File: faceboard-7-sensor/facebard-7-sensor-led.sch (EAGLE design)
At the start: 31 parts, among them Q1 QRE1113, Q2 QRE1113, Q3 QRE1113, Q4 QRE1113, Q5 QRE1113, Q6 QRE1113, Q7 QRE1113, U1 CD4051BE

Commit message: add ffc boards
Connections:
- net N$10 renamed C4
- net N$12 renamed C5
- net N$14 renamed C6
- net N$2 renamed C0
- net N$4 renamed C1
- net N$6 renamed C2
- net N$8 renamed C3
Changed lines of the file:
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@@
 </segment>
 </net>
-<net name="N$2" class="0">
+<net name="C0" class="0">
 <segment>
 <wire x1="20.32" y1="86.36" x2="124.46" y2="86.36" width="0.1524" layer="91"/>
@@
 <wire x1="22.86" y1="157.48" x2="20.32" y2="157.48" width="0.1524" layer="91"/>
 <junction x="22.86" y="157.48"/>
+<label x="124.46" y="63.5" size="1.778" layer="95" xref="yes"/>
 </segment>
 </net>
@@
 </segment>
 </net>
-<net name="N$4" class="0">
+<net name="C1" class="0">
 <segment>
 <pinref part="Q2" gate="A" pin="3"/>
@@
 <wire x1="137.16" y1="93.98" x2="137.16" y2="66.04" width="0.1524" layer="91"/>
 <wire x1="137.16" y1="66.04" x2="109.22" y2="66.04" width="0.1524" layer="91"/>
+<label x="137.16" y="66.04" size="1.778" layer="95" xref="yes"/>
 </segment>
 </net>
@@
 </segment>
 </net>
-<net name="N$6" class="0">
+<net name="C2" class="0">
 <segment>
 <pinref part="Q3" gate="A" pin="3"/>
@@
 <pinref part="U1" gate="A" pin="CHANNELSIN/OUT2"/>
 <wire x1="162.56" y1="68.58" x2="109.22" y2="68.58" width="0.1524" layer="91"/>
+<label x="132.08" y="68.58" size="1.778" layer="95" rot="R90" xref="yes"/>
 </segment>
 </net>
@@
 </segment>
 </net>
-<net name="N$8" class="0">
+<net name="C3" class="0">
 <segment>
 <pinref part="Q4" gate="A" pin="3"/>
@@
 <wire x1="228.6" y1="60.96" x2="109.22" y2="60.96" width="0.1524" layer="91"/>
 <junction x="228.6" y="157.48"/>
+<label x="132.08" y="63.5" size="1.778" layer="95" rot="R270" xref="yes"/>
 </segment>
 </net>
@@
 </segment>
 </net>
-<net name="N$10" class="0">
+<net name="C4" class="0">
 <segment>
 <pinref part="Q5" gate="A" pin="3"/>
@@
 <pinref part="U1" gate="A" pin="CHANNELSIN/OUT4"/>
 <wire x1="2.54" y1="71.12" x2="7.62" y2="71.12" width="0.1524" layer="91"/>
+<label x="5.08" y="71.12" size="1.778" layer="95" rot="R90" xref="yes"/>
 </segment>
 </net>
@@
 </segment>
 </net>
-<net name="N$12" class="0">
+<net name="C5" class="0">
 <segment>
 <pinref part="Q6" gate="A" pin="3"/>
@@
 <wire x1="-5.08" y1="78.74" x2="-5.08" y2="60.96" width="0.1524" layer="91"/>
 <wire x1="-5.08" y1="60.96" x2="7.62" y2="60.96" width="0.1524" layer="91"/>
+<label x="0" y="60.96" size="1.778" layer="95" rot="R270" xref="yes"/>
 </segment>
 </net>
@@
 </segment>
 </net>
-<net name="N$14" class="0">
+<net name="C6" class="0">
 <segment>
 <pinref part="Q7" gate="A" pin="3"/>
@@
 <wire x1="424.18" y1="147.32" x2="426.72" y2="147.32" width="0.1524" layer="91"/>
 <wire x1="426.72" y1="147.32" x2="426.974" y2="80.518" width="0.1524" layer="91"/>
-<wire x1="426.974" y1="80.518" x2="0.254" y2="80.518" width="0.1524" layer="91"/>
-<wire x1="0.254" y1="80.518" x2="0" y2="68.58" width="0.1524" layer="91"/>
+<wire x1="426.974" y1="80.518" x2="0" y2="81.026" width="0.1524" layer="91"/>
+<wire x1="0" y1="81.026" x2="0" y2="68.58" width="0.1524" layer="91"/>
 <pinref part="U1" gate="A" pin="CHANNELSIN/OUT6"/>
 <wire x1="0" y1="68.58" x2="7.62" y2="68.58" width="0.1524" layer="91"/>
-</segment>
-</net>
+<label x="0" y="68.58" size="1.778" layer="95" rot="R180" xref="yes"/>
+</segment>
+</net>

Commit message: routing
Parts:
- SV2: SPICEPREFIX (none) -> X
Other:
- moved on the sheet: D1, D2, D3, D4, D5, D6, D7, U1

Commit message: re-draw schematics
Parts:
- R10: value 10k -> 100k
- SV2: value header -> Output
- SV3: value header -> Input
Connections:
- net LEDDIN renamed N$12
- new net N$14: D1.VSS, D2.VSS, D3.VSS
- new net N$15: D4.VSS
- new net VCC: R1.1, R10.2, R11.1, R12.2, R13.1, R14.2, R2.2, R3.1, R4.2, R5.1, R6.2, R7.1, R8.2, R9.1, SV2.2, SV3.2
- net 5V: no longer R1.1, R10.2, R11.1, R12.2, R13.1, R14.2, R2.2, R3.1, R4.2, R5.1, R6.2, R7.1, R8.2, R9.1, SV2.2, SV3.2
- net C0: now also U1.CH0; no longer U1.CHANNELSIN/OUT0
- net C1: now also U1.CH1; no longer U1.CHANNELSIN/OUT1
- net C2: now also U1.CH2; no longer U1.CHANNELSIN/OUT2
- net C3: now also U1.CH3; no longer U1.CHANNELSIN/OUT3
- net C4: now also U1.CH4; no longer U1.CHANNELSIN/OUT4
- net C5: now also U1.CH5; no longer U1.CHANNELSIN/OUT5
- net C6: now also U1.CH6; no longer U1.CHANNELSIN/OUT6
- net GND: now also U1.GND; no longer D1.VSS, D2.VSS, D3.VSS, D4.VSS, U1.VSS
- net SIG: now also U1.COM; no longer U1.COMOUT/IN
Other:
- moved on the sheet: D1, D2, D3, D4, D5, D6, D7, R1, R10, R11, R12, R13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

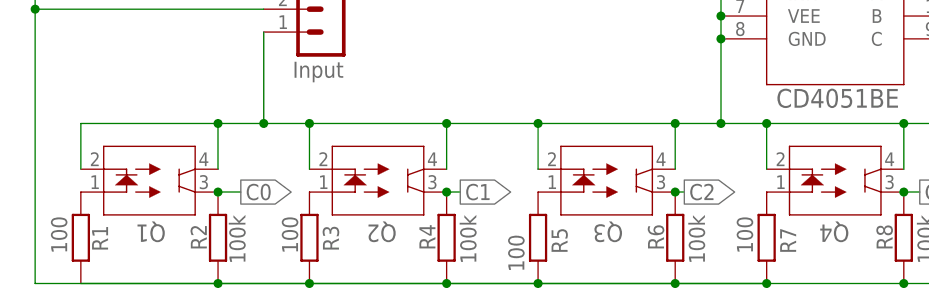
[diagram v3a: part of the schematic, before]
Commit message: fix vcc net
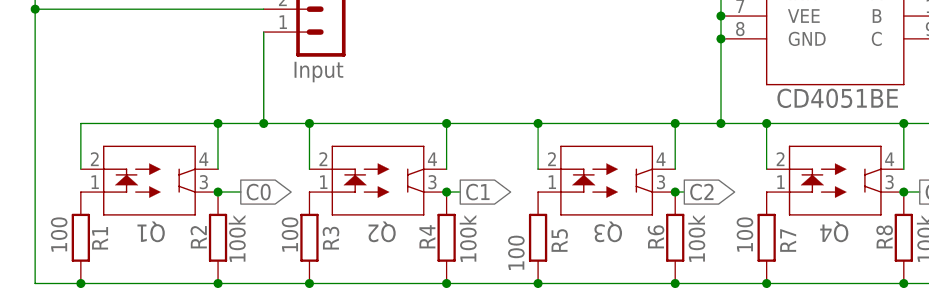
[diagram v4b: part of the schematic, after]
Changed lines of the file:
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@@
 <net name="VCC" class="0">
 <segment>
+<pinref part="SUPPLY2" gate="G$1" pin="VCC"/>
+<wire x1="-22.86" y1="91.44" x2="-22.86" y2="132.08" width="0.1524" layer="91"/>
+<pinref part="SV3" gate="1" pin="2"/>
+<wire x1="2.54" y1="91.44" x2="-22.86" y2="91.44" width="0.1524" layer="91"/>
+<junction x="-22.86" y="91.44"/>
+<wire x1="-22.86" y1="60.96" x2="-22.86" y2="91.44" width="0.1524" layer="91"/>
+<wire x1="162.56" y1="91.44" x2="162.56" y2="60.96" width="0.1524" layer="91"/>
+<pinref part="SV2" gate="1" pin="2"/>
+<wire x1="162.56" y1="91.44" x2="129.54" y2="91.44" width="0.1524" layer="91"/>
+<wire x1="162.56" y1="60.96" x2="149.86" y2="60.96" width="0.1524" layer="91"/>
 <pinref part="R1" gate="G$1" pin="1"/>
-<wire x1="-17.78" y1="60.96" x2="-2.54" y2="60.96" width="0.1524" layer="91"/>
-<pinref part="R2" gate="G$1" pin="2"/>
-<junction x="-2.54" y="60.96"/>
-<wire x1="-2.54" y1="60.96" x2="7.62" y2="60.96" width="0.1524" layer="91"/>
-<pinref part="R3" gate="G$1" pin="1"/>
-<junction x="7.62" y="60.96"/>
-<wire x1="7.62" y1="60.96" x2="22.86" y2="60.96" width="0.1524" layer="91"/>
-<pinref part="R4" gate="G$1" pin="2"/>
-<junction x="22.86" y="60.96"/>
-<wire x1="22.86" y1="60.96" x2="33.02" y2="60.96" width="0.1524" layer="91"/>
-<pinref part="R5" gate="G$1" pin="1"/>
-<junction x="33.02" y="60.96"/>
-<wire x1="33.02" y1="60.96" x2="48.26" y2="60.96" width="0.1524" layer="91"/>
-<pinref part="R6" gate="G$1" pin="2"/>
-<junction x="48.26" y="60.96"/>
-<wire x1="48.26" y1="60.96" x2="58.42" y2="60.96" width="0.1524" layer="91"/>
-<pinref part="R7" gate="G$1" pin="1"/>
-<junction x="58.42" y="60.96"/>
-<wire x1="58.42" y1="60.96" x2="-22.86" y2="60.96" width="0.1524" layer="91"/>
-<pinref part="R14" gate="G$1" pin="2"/>
 <wire x1="149.86" y1="60.96" x2="134.62" y2="60.96" width="0.1524" layer="91"/>
-<pinref part="R13" gate="G$1" pin="1"/>
 <wire x1="134.62" y1="60.96" x2="124.46" y2="60.96" width="0.1524" layer="91"/>
 <wire x1="124.46" y1="60.96" x2="109.22" y2="60.96" width="0.1524" layer="91"/>
@@
 <wire x1="83.82" y1="60.96" x2="73.66" y2="60.96" width="0.1524" layer="91"/>
 <wire x1="73.66" y1="60.96" x2="58.42" y2="60.96" width="0.1524" layer="91"/>
-<junction x="134.62" y="60.96"/>
+<wire x1="58.42" y1="60.96" x2="48.26" y2="60.96" width="0.1524" layer="91"/>
+<wire x1="48.26" y1="60.96" x2="33.02" y2="60.96" width="0.1524" layer="91"/>
+<wire x1="33.02" y1="60.96" x2="22.86" y2="60.96" width="0.1524" layer="91"/>
+<wire x1="22.86" y1="60.96" x2="7.62" y2="60.96" width="0.1524" layer="91"/>
+<wire x1="7.62" y1="60.96" x2="-2.54" y2="60.96" width="0.1524" layer="91"/>
+<wire x1="-2.54" y1="60.96" x2="-17.78" y2="60.96" width="0.1524" layer="91"/>
+<wire x1="-17.78" y1="60.96" x2="-22.86" y2="60.96" width="0.1524" layer="91"/>
+<junction x="-17.78" y="60.96"/>
+<pinref part="R2" gate="G$1" pin="2"/>
+<junction x="-2.54" y="60.96"/>
+<pinref part="R3" gate="G$1" pin="1"/>
+<junction x="7.62" y="60.96"/>
+<pinref part="R4" gate="G$1" pin="2"/>
+<junction x="22.86" y="60.96"/>
+<pinref part="R5" gate="G$1" pin="1"/>
+<junction x="33.02" y="60.96"/>
+<pinref part="R6" gate="G$1" pin="2"/>
+<junction x="48.26" y="60.96"/>
+<pinref part="R7" gate="G$1" pin="1"/>
+<junction x="58.42" y="60.96"/>
+<pinref part="R8" gate="G$1" pin="2"/>
+<junction x="73.66" y="60.96"/>
+<pinref part="R9" gate="G$1" pin="1"/>
+<junction x="83.82" y="60.96"/>
+<pinref part="R10" gate="G$1" pin="2"/>
+<junction x="99.06" y="60.96"/>
+<pinref part="R11" gate="G$1" pin="1"/>
+<junction x="109.22" y="60.96"/>
 <pinref part="R12" gate="G$1" pin="2"/>
 <junction x="124.46" y="60.96"/>
-<pinref part="R11" gate="G$1" pin="1"/>
-<junction x="109.22" y="60.96"/>
-<pinref part="R10" gate="G$1" pin="2"/>
-<junction x="99.06" y="60.96"/>
-<pinref part="R9" gate="G$1" pin="1"/>
-<junction x="83.82" y="60.96"/>
-<pinref part="R8" gate="G$1" pin="2"/>
-<junction x="73.66" y="60.96"/>
-<pinref part="SUPPLY2" gate="G$1" pin="VCC"/>
-<wire x1="-22.86" y1="60.96" x2="-22.86" y2="91.44" width="0.1524" layer="91"/>
-<pinref part="SV3" gate="1" pin="2"/>
-<wire x1="-22.86" y1="91.44" x2="-22.86" y2="132.08" width="0.1524" layer="91"/>
-<wire x1="2.54" y1="91.44" x2="-22.86" y2="91.44" width="0.1524" layer="91"/>
-<junction x="-22.86" y="91.44"/>
-<wire x1="162.56" y1="91.44" x2="162.56" y2="60.96" width="0.1524" layer="91"/>
-<wire x1="162.56" y1="60.96" x2="149.86" y2="60.96" width="0.1524" layer="91"/>
+<pinref part="R13" gate="G$1" pin="1"/>
+<junction x="134.62" y="60.96"/>
+<pinref part="R14" gate="G$1" pin="2"/>
 <junction x="149.86" y="60.96"/>
-<pinref part="SV2" gate="1" pin="2"/>
-<wire x1="162.56" y1="91.44" x2="129.54" y2="91.44" width="0.1524" layer="91"/>
 </segment>
 </net>

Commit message: add din dout labels
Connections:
- net LEDDOUT renamed DOUT
- net N$12 renamed DIN
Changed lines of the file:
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@@
 </segment>
 </net>
-<net name="LEDDOUT" class="0">
+<net name="DOUT" class="0">
 <segment>
 <pinref part="D7" gate="G$1" pin="DOUT"/>
@@
 <wire x1="139.7" y1="119.38" x2="139.7" y2="104.14" width="0.1524" layer="91"/>
 <wire x1="139.7" y1="104.14" x2="129.54" y2="104.14" width="0.1524" layer="91"/>
+<label x="139.446" y="108.712" size="1.778" layer="95" rot="R90"/>
 </segment>
 </net>
@@
 </segment>
 </net>
-<net name="N$12" class="0">
+<net name="DIN" class="0">
 <segment>
 <pinref part="D1" gate="G$1" pin="DIN"/>
@@
 <wire x1="-7.62" y1="104.14" x2="-7.62" y2="119.38" width="0.1524" layer="91"/>
 <wire x1="-7.62" y1="119.38" x2="-5.842" y2="119.38" width="0.1524" layer="91"/>
+<label x="-7.874" y="109.22" size="1.778" layer="95" rot="R90"/>
 </segment>
 </net>

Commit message: tidy
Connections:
- removed net 5V: U1.VDD
- net VCC: now also U1.VDD
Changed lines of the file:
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@@
 </instance>
 <instance part="R1" gate="G$1" x="-17.78" y="66.04" smashed="yes" rot="MR90">
-<attribute name="NAME" x="-16.5354" y="64.516" size="1.778" layer="95" rot="MR90"/>
+<attribute name="NAME" x="-16.7894" y="64.516" size="1.778" layer="95" rot="MR90"/>
 <attribute name="VALUE" x="-21.082" y="64.262" size="1.778" layer="96" rot="MR90"/>
 </instance>
@@
 </instance>
 <instance part="R3" gate="G$1" x="7.62" y="66.04" smashed="yes" rot="MR90">
-<attribute name="NAME" x="9.1186" y="64.516" size="1.778" layer="95" rot="MR90"/>
+<attribute name="NAME" x="8.8646" y="64.516" size="1.778" layer="95" rot="MR90"/>
 <attribute name="VALUE" x="4.572" y="64.262" size="1.778" layer="96" rot="MR90"/>
 </instance>
@@
 <instance part="R5" gate="G$1" x="33.02" y="66.04" smashed="yes" rot="MR90">
 <attribute name="NAME" x="34.5186" y="64.262" size="1.778" layer="95" rot="MR90"/>
-<attribute name="VALUE" x="29.718" y="62.23" size="1.778" layer="96" rot="MR90"/>
+<attribute name="VALUE" x="29.972" y="63.754" size="1.778" layer="96" rot="MR90"/>
 </instance>
 <instance part="R6" gate="G$1" x="48.26" y="66.04" smashed="yes" rot="MR270">
@@
 </instance>
 <instance part="R7" gate="G$1" x="58.42" y="66.04" smashed="yes" rot="MR90">
-<attribute name="NAME" x="59.9186" y="64.262" size="1.778" layer="95" rot="MR90"/>
+<attribute name="NAME" x="59.6646" y="64.77" size="1.778" layer="95" rot="MR90"/>
 <attribute name="VALUE" x="55.118" y="64.262" size="1.778" layer="96" rot="MR90"/>
 </instance>
@@
 </instance>
 <instance part="R10" gate="G$1" x="99.06" y="66.04" smashed="yes" rot="MR270">
-<attribute name="NAME" x="97.8154" y="68.58" size="1.778" layer="95" rot="MR270"/>
+<attribute name="NAME" x="97.8154" y="68.072" size="1.778" layer="95" rot="MR270"/>
 <attribute name="VALUE" x="102.362" y="68.58" size="1.778" layer="96" rot="MR270"/>
 </instance>
@@
 </instance>
 <instance part="R11" gate="G$1" x="109.22" y="66.04" smashed="yes" rot="MR90">
-<attribute name="NAME" x="110.4646" y="64.262" size="1.778" layer="95" rot="MR90"/>
+<attribute name="NAME" x="110.4646" y="64.008" size="1.778" layer="95" rot="MR90"/>
 <attribute name="VALUE" x="105.918" y="64.008" size="1.778" layer="96" rot="MR90"/>
 </instance>
 <instance part="R12" gate="G$1" x="124.46" y="66.04" smashed="yes" rot="MR270">
-<attribute name="NAME" x="123.2154" y="68.58" size="1.778" layer="95" rot="MR270"/>
+<attribute name="NAME" x="123.2154" y="68.326" size="1.778" layer="95" rot="MR270"/>
 <attribute name="VALUE" x="127.762" y="68.58" size="1.778" layer="96" rot="MR270"/>
 </instance>
@@
 </instance>
 <instance part="R14" gate="G$1" x="149.86" y="66.04" smashed="yes" rot="MR270">
-<attribute name="NAME" x="148.6154" y="68.58" size="1.778" layer="95" rot="MR270"/>
+<attribute name="NAME" x="148.6154" y="68.326" size="1.778" layer="95" rot="MR270"/>
 <attribute name="VALUE" x="153.162" y="68.58" size="1.778" layer="96" rot="MR270"/>
 </instance>
@@
 </segment>
 </net>
-<net name="5V" class="0">
-<segment>
-<wire x1="78.74" y1="105.918" x2="84.328" y2="105.918" width="0.1524" layer="91"/>
-<label x="84.328" y="105.918" size="1.778" layer="95" xref="yes"/>
-<pinref part="U1" gate="A" pin="VDD"/>
-</segment>
-</net>
 <net name="A" class="0">
 <segment>
@@
 <junction x="149.86" y="60.96"/>
 </segment>
-</net>
+<segment>
+<wire x1="78.74" y1="105.918" x2="84.328" y2="105.918" width="0.1524" layer="91"/>
+<label x="84.328" y="105.918" size="1.778" layer="95" xref="yes"/>
+<pinref part="U1" gate="A" pin="VDD"/>
+</segment>
+</net>
